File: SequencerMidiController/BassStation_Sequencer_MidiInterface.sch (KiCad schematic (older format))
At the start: 0 parts

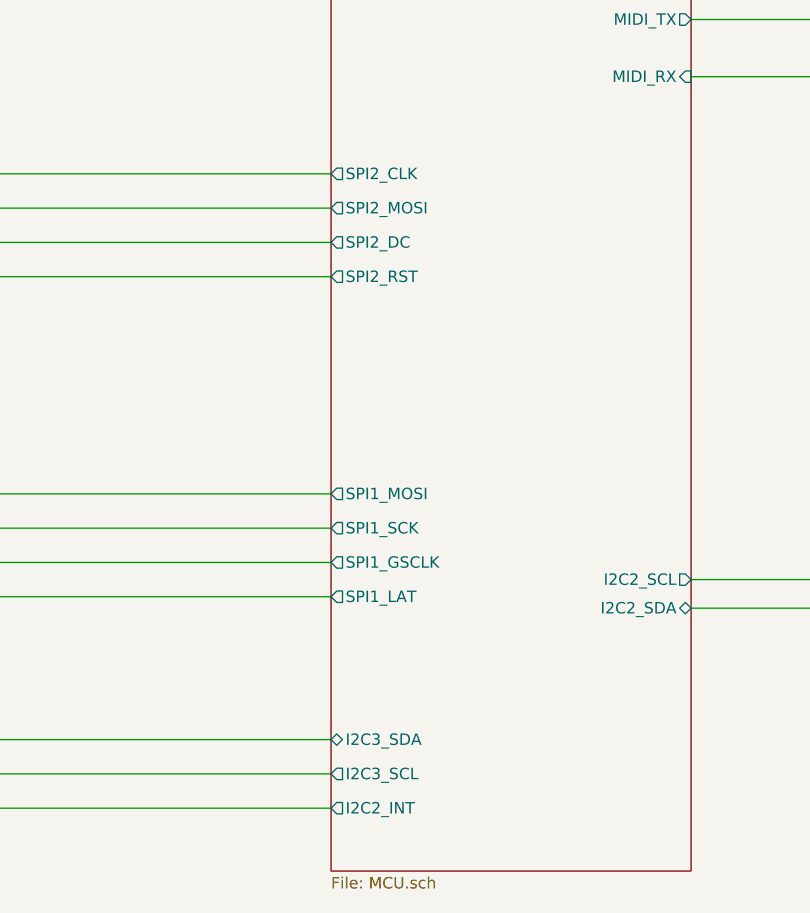
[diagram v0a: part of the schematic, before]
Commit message: RevA Layout draft completed
- Needs tidy up
- Add test points
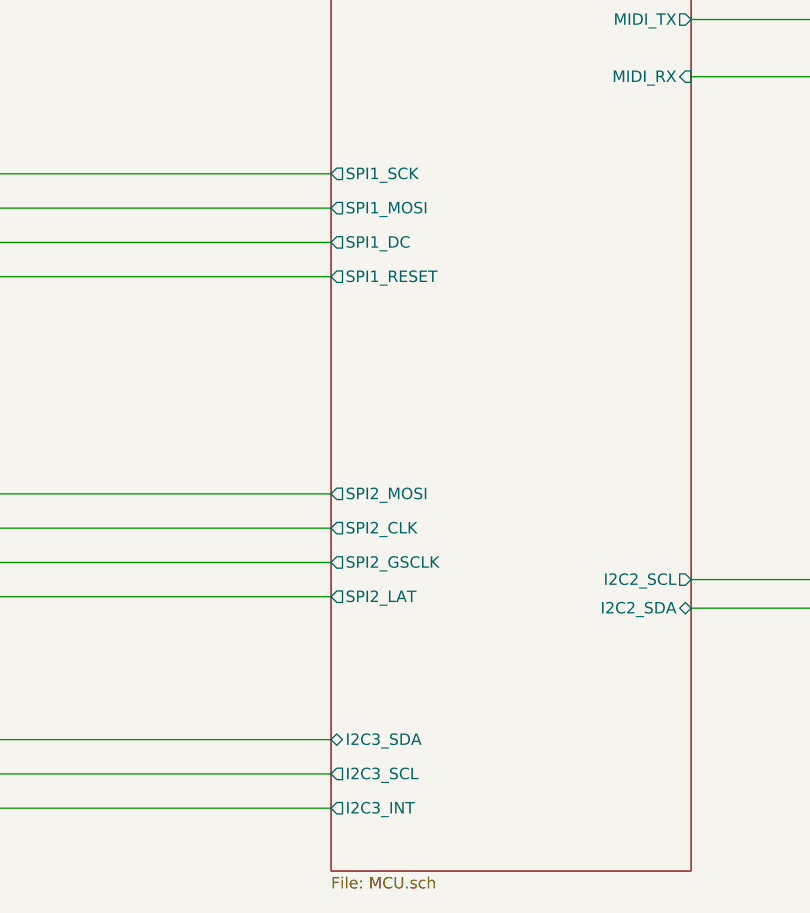
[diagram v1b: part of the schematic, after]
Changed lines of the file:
@@
 F3 "MIDI_RX" I R 9850 3825 50
 F4 "MIDI_TX" O R 9850 3575 50
-F5 "SPI2_MOSI" O L 8275 4400 50
-F6 "SPI2_CLK" O L 8275 4250 50
+F5 "SPI2_MOSI" O L 8275 5650 50
+F6 "SPI2_CLK" O L 8275 5800 50
 F7 "I2C2_SDA" B R 9850 6150 50
 F8 "I2C2_SCL" O R 9850 6025 50
-F9 "SPI1_MOSI" O L 8275 5650 50
-F10 "SPI1_SCK" O L 8275 5800 50
-F11 "SPI1_GSCLK" O L 8275 5950 50
-F12 "SPI1_LAT" O L 8275 6100 50
-F13 "I2C3_SDA" B L 8275 6725 50
-F14 "I2C3_SCL" O L 8275 6875 50
-F15 "I2C2_INT" O L 8275 7025 50
-F16 "SPI2_DC" O L 8275 4550 50
-F17 "SPI2_RST" O L 8275 4700 50
+F9 "SPI1_MOSI" O L 8275 4400 50
+F10 "SPI1_SCK" O L 8275 4250 50
+F11 "I2C3_SDA" B L 8275 6725 50
+F12 "I2C3_SCL" O L 8275 6875 50
+F13 "SPI2_LAT" O L 8275 6100 50
+F14 "SPI2_GSCLK" O L 8275 5950 50
+F15 "SPI1_DC" O L 8275 4550 50
+F16 "SPI1_RESET" O L 8275 4700 50
+F17 "I2C3_INT" O L 8275 7025 50
 $EndSheet
 $Sheet
